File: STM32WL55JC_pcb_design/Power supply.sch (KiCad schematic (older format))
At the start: 18 parts

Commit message: First pcb commit
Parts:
- IC?: symbol RT9058-33GX:RT9058-33GX -> STM32WL55JC_pcb_design-rescue:RT9058-33GX-RT9058-33GX
- J? (x2): symbol CT3151-2:CT3151-2 -> STM32WL55JC_pcb_design-rescue:CT3151-2-CT3151-2
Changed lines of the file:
@@
 	3900 2050 3900 2300
 $Comp
-L RT9058-33GX:RT9058-33GX IC?
+L STM32WL55JC_pcb_design-rescue:RT9058-33GX-RT9058-33GX IC?
 U 1 1 612D32E8
 P 7100 1900
@@
 NoConn ~ 8300 2000
 $Comp
-L CT3151-2:CT3151-2 J?
+L STM32WL55JC_pcb_design-rescue:CT3151-2-CT3151-2 J?
 U 1 1 612D4BF0
 P 3600 2300
@@
 $EndComp
 $Comp
-L CT3151-2:CT3151-2 J?
+L STM32WL55JC_pcb_design-rescue:CT3151-2-CT3151-2 J?
 U 1 1 612D8B84
 P 3600 2550

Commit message: Complete first version - todo: rf pins
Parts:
- added C? (x2): 10uF, symbol Device:C
- added U?: L78M05ABDT-TR, VREG_L78M05ABDT-TR, symbol L78M05ABDT-TR:L78M05ABDT-TR
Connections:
- net labels added: 29V5, 5V
- wire segments 67 -> 80
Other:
- moved on the sheet: C?, D?, FB?, IC?, J?, Q?, R?, U?

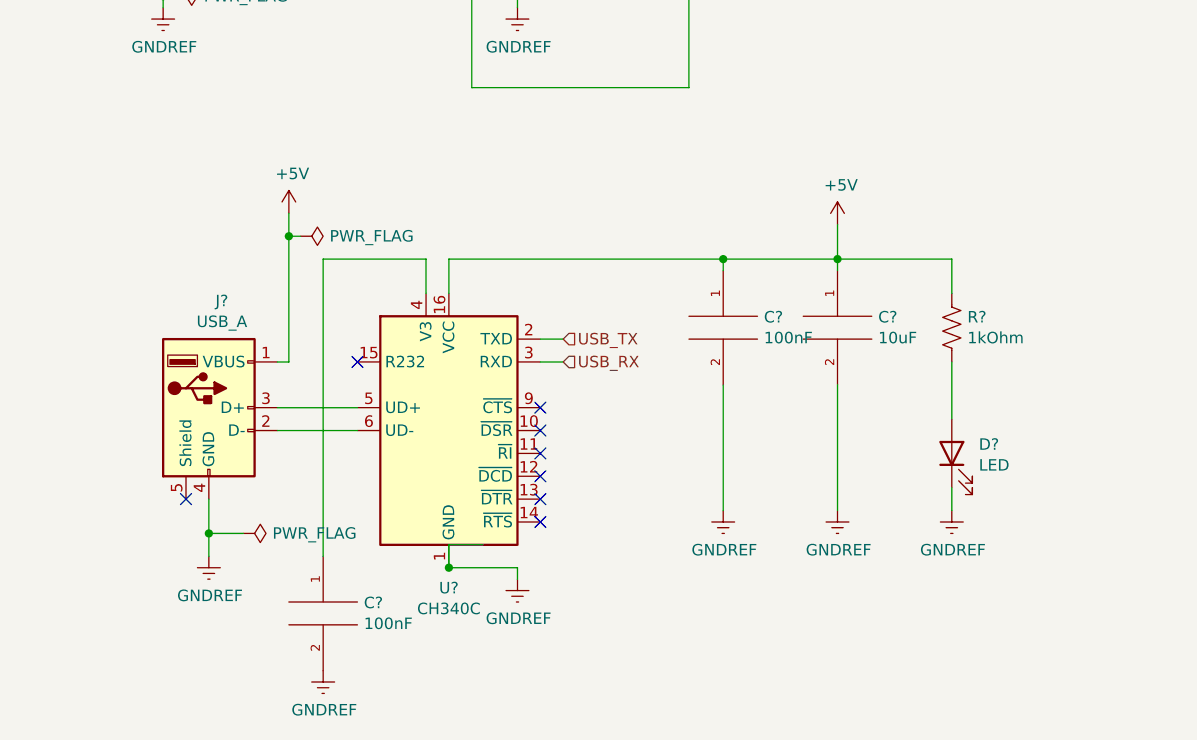
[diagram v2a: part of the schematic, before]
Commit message: Add temperature and humidty sensor, add rf connections
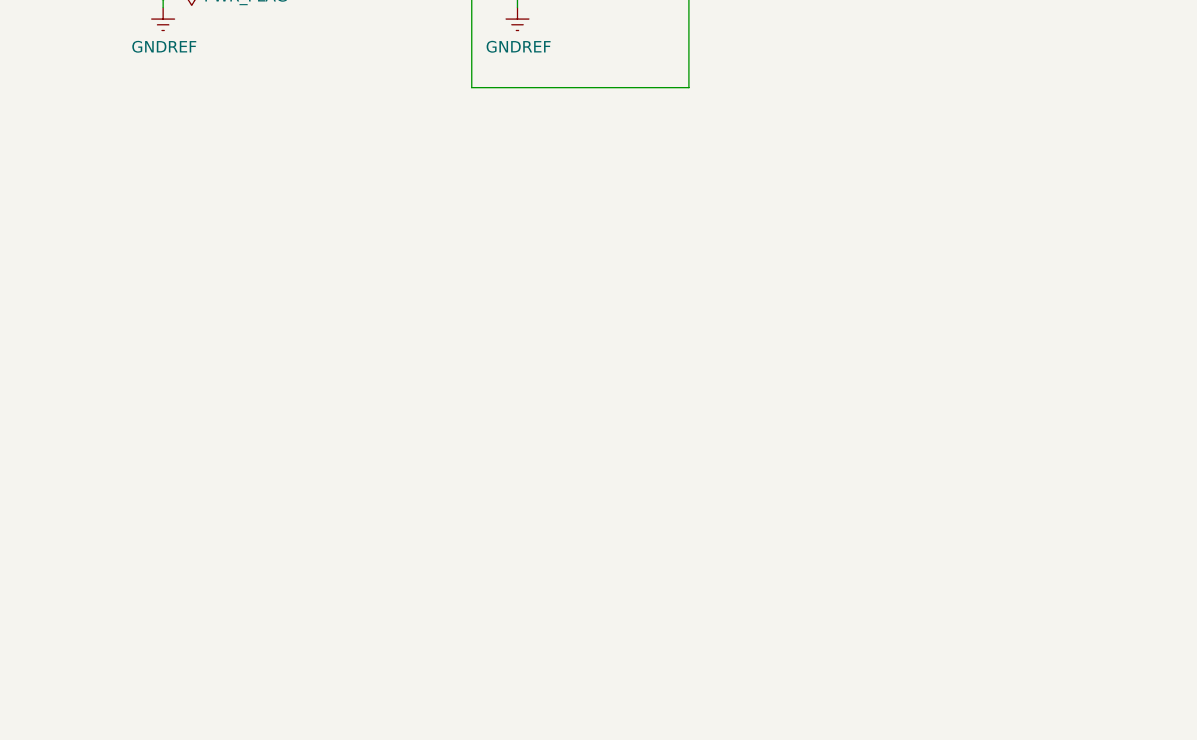
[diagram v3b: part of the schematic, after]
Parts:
- removed C?: 10uF, symbol pspice:CAP
- removed C? (x2): 100nF, symbol pspice:CAP
- removed D?: LED, symbol Device:LED
- removed J?: USB_A, symbol Connector:USB_A
- removed R?: 1kOhm, symbol Device:R_US
- removed U?: CH340C, Package_SO:SOIC-16_3.9x9.9mm_P1.27mm, symbol Interface_USB:CH340C
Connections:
- net labels removed: USB_RX, USB_TX
- wire segments 80 -> 50
- no-connect marks 9 -> 1

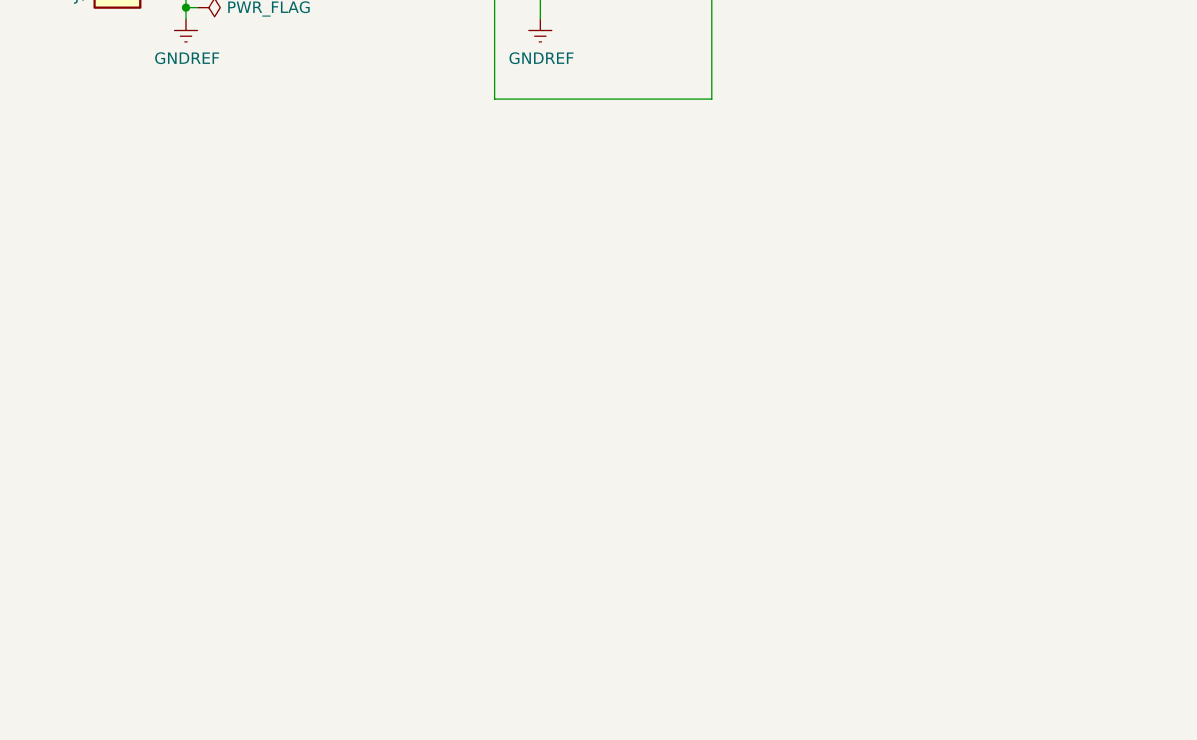
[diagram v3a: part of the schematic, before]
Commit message: Finish RF matching network
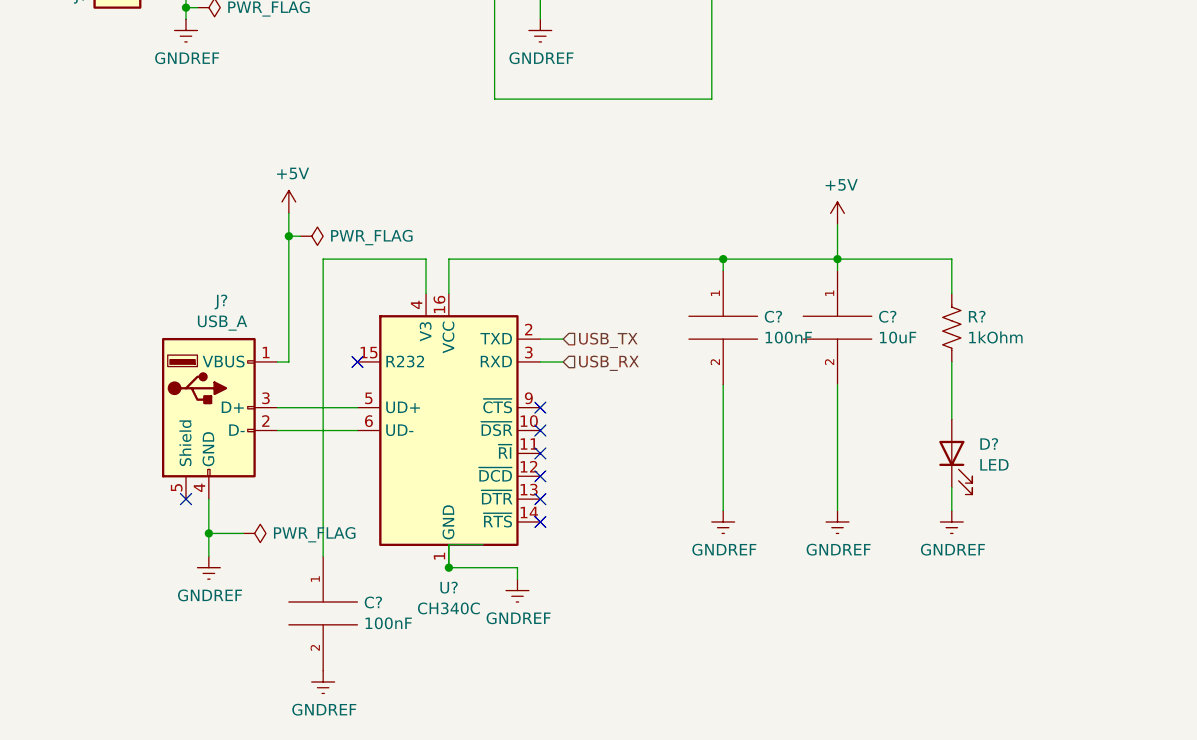
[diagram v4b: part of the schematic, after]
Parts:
- added C?: 10uF, symbol pspice:CAP
- added C? (x2): 100nF, symbol pspice:CAP
- added D?: LED, symbol Device:LED
- added J?: USB_A, symbol Connector:USB_A
- added R?: 1kOhm, symbol Device:R_US
- added U?: CH340C, Package_SO:SOIC-16_3.9x9.9mm_P1.27mm, symbol Interface_USB:CH340C
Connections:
- net labels added: USB_RX, USB_TX
- wire segments 50 -> 80
- no-connect marks 1 -> 9

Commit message: Update ADC section to work with MAX11635
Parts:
- removed C?: 100nF, symbol Device:C
- C? (x2): value 10uF -> 1uF
- C?: value 10uF -> 0.33uF
- C?: value 10uF -> 100nF
- U?: symbol L78M05ABDT-TR:L78M05ABDT-TR -> STM32WL55JC_pcb_design-rescue:L78M05ABDT-TR-L78M05ABDT-TR
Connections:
- net labels removed: USB_RX, USB_TX
- wire segments 80 -> 74
- no-connect marks 9 -> 11
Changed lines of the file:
@@
 $Descr A4 11693 8268
 encoding utf-8
-Sheet 6 6
+Sheet 5 6
 Title ""
 Date ""
@@
 P 6200 2800
 F 0 "C?" H 6315 2846 50  0000 L CNN
-F 1 "10uF" H 6315 2755 50  0000 L CNN
+F 1 "1uF" H 6315 2755 50  0000 L CNN
 F 2 "" H 6238 2650 50  0001 C CNN
 F 3 "~" H 6200 2800 50  0001 C CNN
@@
 P 7950 2800
 F 0 "C?" H 8065 2846 50  0000 L CNN
-F 1 "10uF" H 8065 2755 50  0000 L CNN
+F 1 "1uF" H 8065 2755 50  0000 L CNN
 F 2 "" H 7988 2650 50  0001 C CNN
 F 3 "~" H 7950 2800 50  0001 C CNN
@@
 	1    0    0    -1
 $EndComp
-Wire Wire Line
-	8350 2500 8500 2500
-$Comp
-L Device:C C?
-U 1 1 613555C4
-P 8350 2800
-F 0 "C?" H 8465 2846 50  0000 L CNN
-F 1 "100nF" H 8465 2755 50  0000 L CNN
-F 2 "" H 8388 2650 50  0001 C CNN
-F 3 "~" H 8350 2800 50  0001 C CNN
-	1    8350 2800
-	1    0    0    -1
-$EndComp
-Wire Wire Line
-	7950 3000 8350 3000
-Wire Wire Line
-	8350 3000 8350 2950
 Connection ~ 7950 3000
-Wire Wire Line
-	8350 2650 8350 2500
-Wire Wire Line
-	8350 2500 7950 2500
 Connection ~ 7950 2500
-Connection ~ 8350 2500
 Wire Wire Line
 	4550 2500 4700 2500
@@
 $EndComp
 Wire Wire Line
-	8350 3000 8500 3000
-Connection ~ 8350 3000
-Wire Wire Line
 	3350 2500 3350 2300
 Connection ~ 3350 2500
@@
 29V5
 $Comp
-L L78M05ABDT-TR:L78M05ABDT-TR U?
+L STM32WL55JC_pcb_design-rescue:L78M05ABDT-TR-L78M05ABDT-TR U?
 U 1 1 61387D5B
 P 7150 1600
+AR Path="/61387D5B" Ref="U?"  Part="1"
+AR Path="/612BE788/61387D5B" Ref="U?"  Part="1"
 F 0 "U?" H 7150 1967 50  0000 C CNN
 F 1 "L78M05ABDT-TR" H 7150 1876 50  0000 C CNN
@@
 P 6400 1750
 F 0 "C?" H 6515 1796 50  0000 L CNN
-F 1 "10uF" H 6515 1705 50  0000 L CNN
+F 1 "0.33uF" H 6515 1705 50  0000 L CNN
 F 2 "" H 6438 1600 50  0001 C CNN
 F 3 "~" H 6400 1750 50  0001 C CNN
@@
 P 8000 1750
 F 0 "C?" H 8115 1796 50  0000 L CNN
-F 1 "10uF" H 8115 1705 50  0000 L CNN
+F 1 "100nF" H 8115 1705 50  0000 L CNN
 F 2 "" H 8038 1600 50  0001 C CNN
 F 3 "~" H 8000 1750 50  0001 C CNN
@@
 	1    0    0    -1
 $EndComp
-Wire Wire Line
-	4900 4700 5000 4700
-Wire Wire Line
-	4900 4800 5000 4800
 Wire Wire Line
 	6200 4200 6200 4350
@@
 	1    0    0    -1
 $EndComp
-Text HLabel 5000 4700 2    50   Input ~ 0
-USB_TX
-Text HLabel 5000 4800 2    50   Input ~ 0
-USB_RX
+NoConn ~ 4900 4700
+NoConn ~ 4900 4800
+Wire Wire Line
+	7950 2500 8500 2500
+Wire Wire Line
+	7950 3000 8500 3000
 $EndSCHEMATC

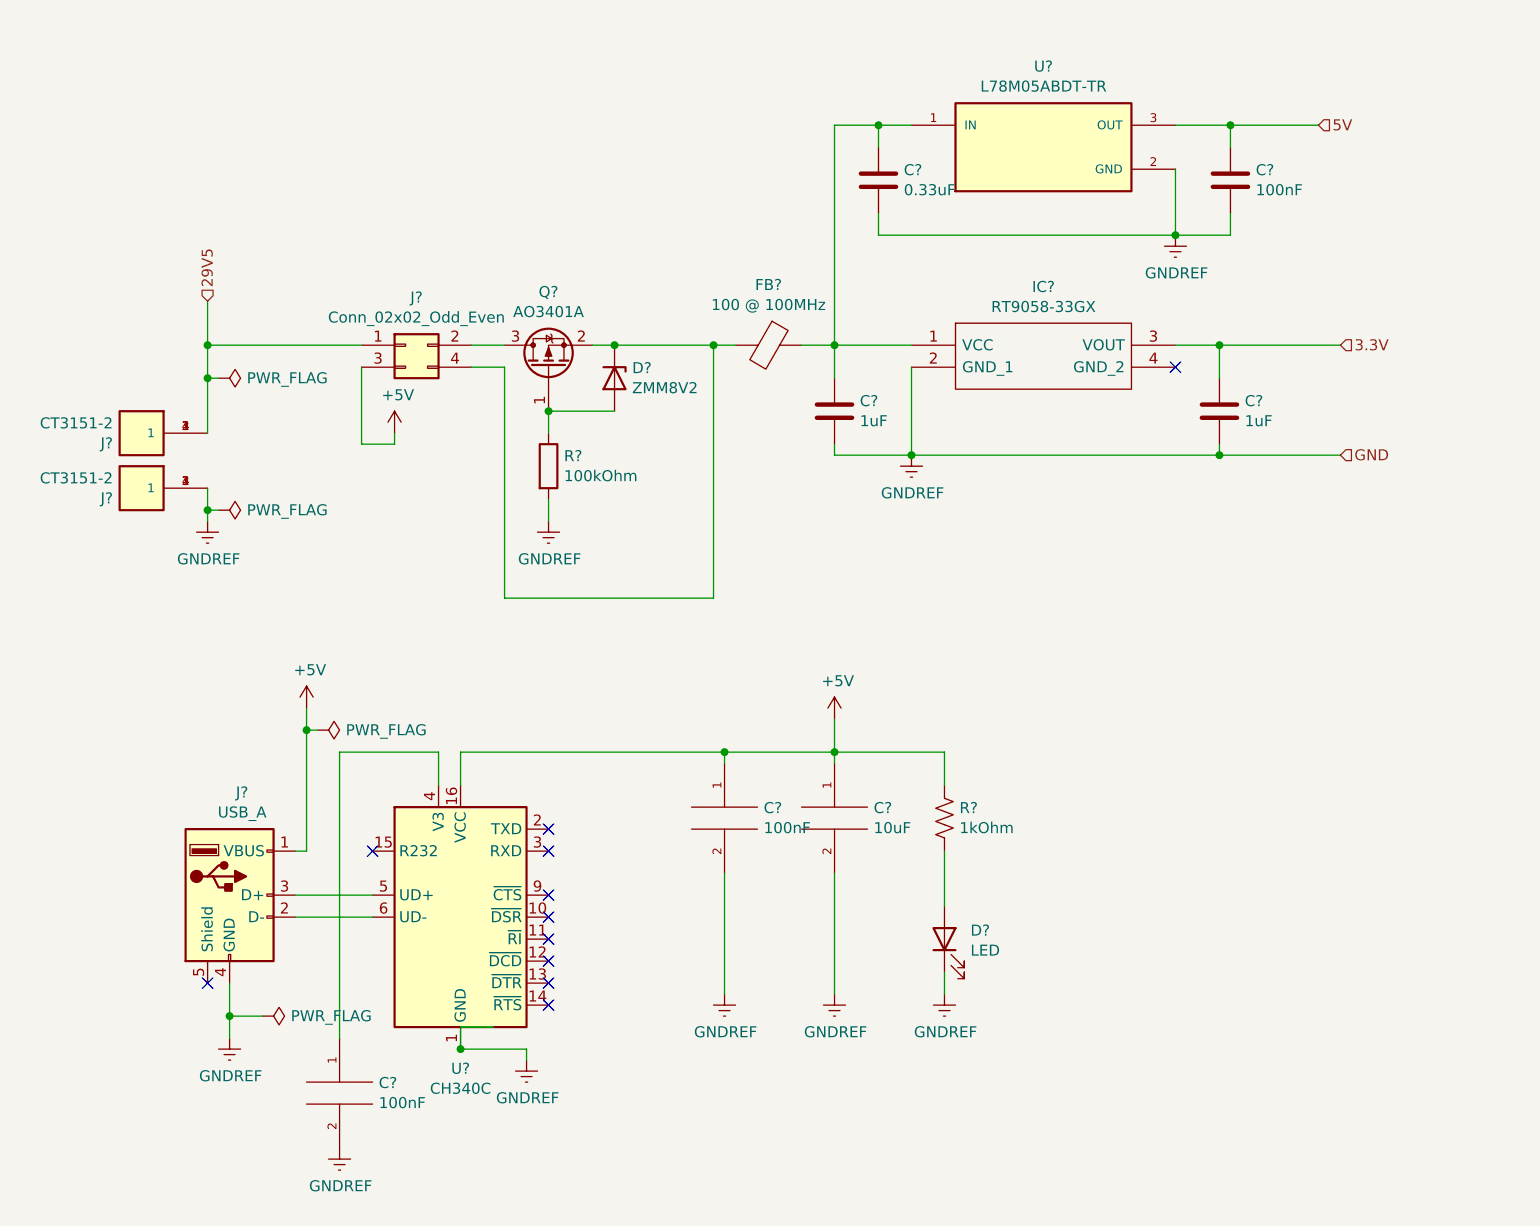
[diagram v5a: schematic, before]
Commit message: Finish component selection and footprint assignment
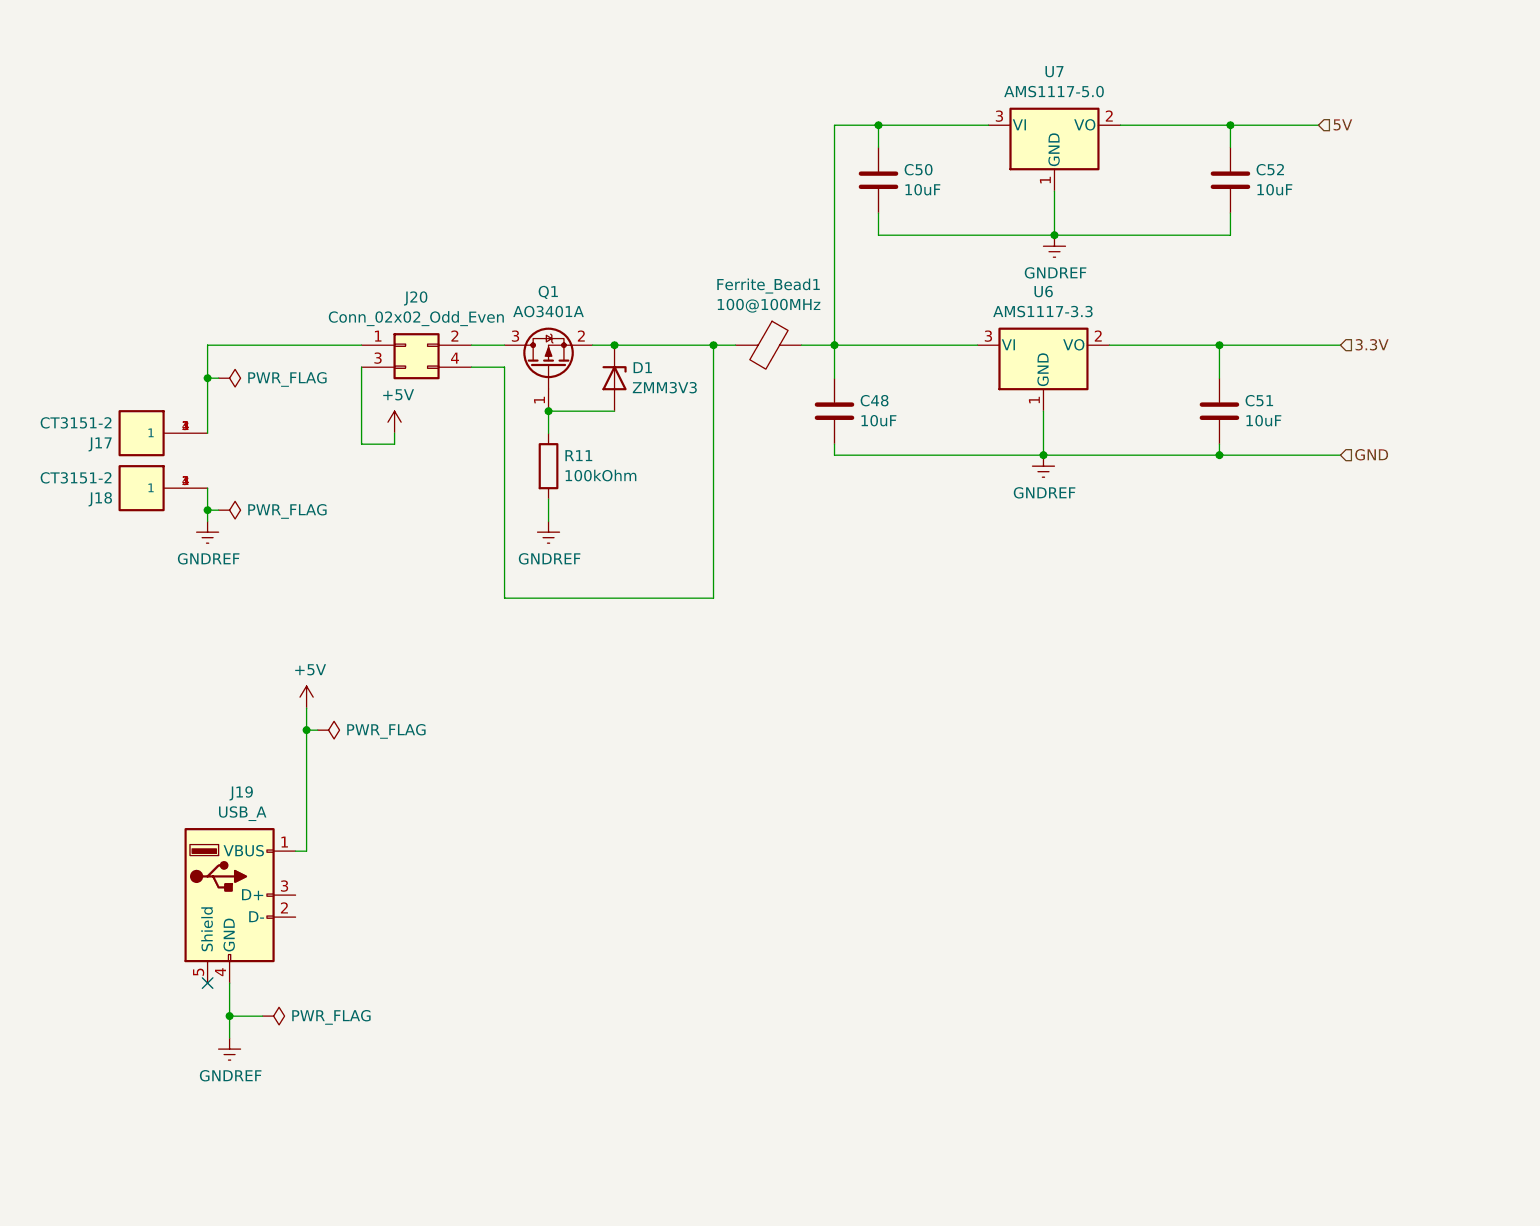
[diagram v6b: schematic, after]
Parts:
- removed C?: 10uF, symbol pspice:CAP
- removed C? (x2): 100nF, symbol pspice:CAP
- removed D?: LED, symbol Device:LED
- removed FB?: 100 @ 100MHz, symbol Device:Ferrite_Bead
- removed IC?: RT9058-33GX, RT905833GX, symbol STM32WL55JC_pcb_design-rescue:RT9058-33GX-RT9058-33GX
- removed R?: 1kOhm, symbol Device:R_US
- removed U?: L78M05ABDT-TR, VREG_L78M05ABDT-TR, symbol STM32WL55JC_pcb_design-rescue:L78M05ABDT-TR-L78M05ABDT-TR
- removed U?: CH340C, Package_SO:SOIC-16_3.9x9.9mm_P1.27mm, symbol Interface_USB:CH340C
- added Ferrite_Bead1: 100@100MHz, Inductor_SMD:L_0805_2012Metric, symbol Device:Ferrite_Bead
- added U6: AMS1117-3.3, Package_TO_SOT_SMD:SOT-223-3_TabPin2, symbol Regulator_Linear:AMS1117-3.3
- added U7: AMS1117-5.0, Package_TO_SOT_SMD:SOT-223-3_TabPin2, symbol Regulator_Linear:AMS1117-5.0
- C48, C51: renamed from C?; value 1uF -> 10uF; footprint (none) -> Capacitor_SMD:C_0805_2012Metric
- C50: renamed from C?; value 0.33uF -> 10uF; footprint (none) -> Capacitor_SMD:C_0805_2012Metric
- C52: renamed from C?; value 100nF -> 10uF; footprint (none) -> Capacitor_SMD:C_0805_2012Metric
- D1: renamed from D?; value ZMM8V2 -> ZMM3V3
- J17, J18: renamed from J?; footprint CALTEST_CT3151-2 -> CT3151-2:CALTEST_CT3151-2
- J19: renamed from J?; footprint (none) -> USBASFBTH:USBASFBTH
- J20: renamed from J?; footprint (none) -> Connector_PinHeader_2.54mm:PinHeader_2x02_P2.54mm_Vertical_SMD
- R11: renamed from R?; footprint (none) -> Resistor_SMD:R_0805_2012Metric
- gave numbers to parts that had none: 1
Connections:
- net 3.3V: now also U6.2 (VO)
- net 5V: now also U7.2 (VO)
- net GNDREF: now also U6.1 (GND), U7.1 (GND)
- net at C48.1, C50.1: now also Ferrite_Bead1.1, U6.3 (VI), U7.3 (VI)
- net at D1.1 (K), J20.4 (Pin_4), Q1.2 (S): now also Ferrite_Bead1.2
- net 29V5: no longer names the net of J17.1, J17.2 (1), J17.3 (1), J17.4 (1), J20.1 (Pin_1)
- no-connect marks 11 -> 1
